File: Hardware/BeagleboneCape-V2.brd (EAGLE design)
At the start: 73.6 x 58.1 mm, 11 parts, among them P8 HEADER1, P9 HEADER2

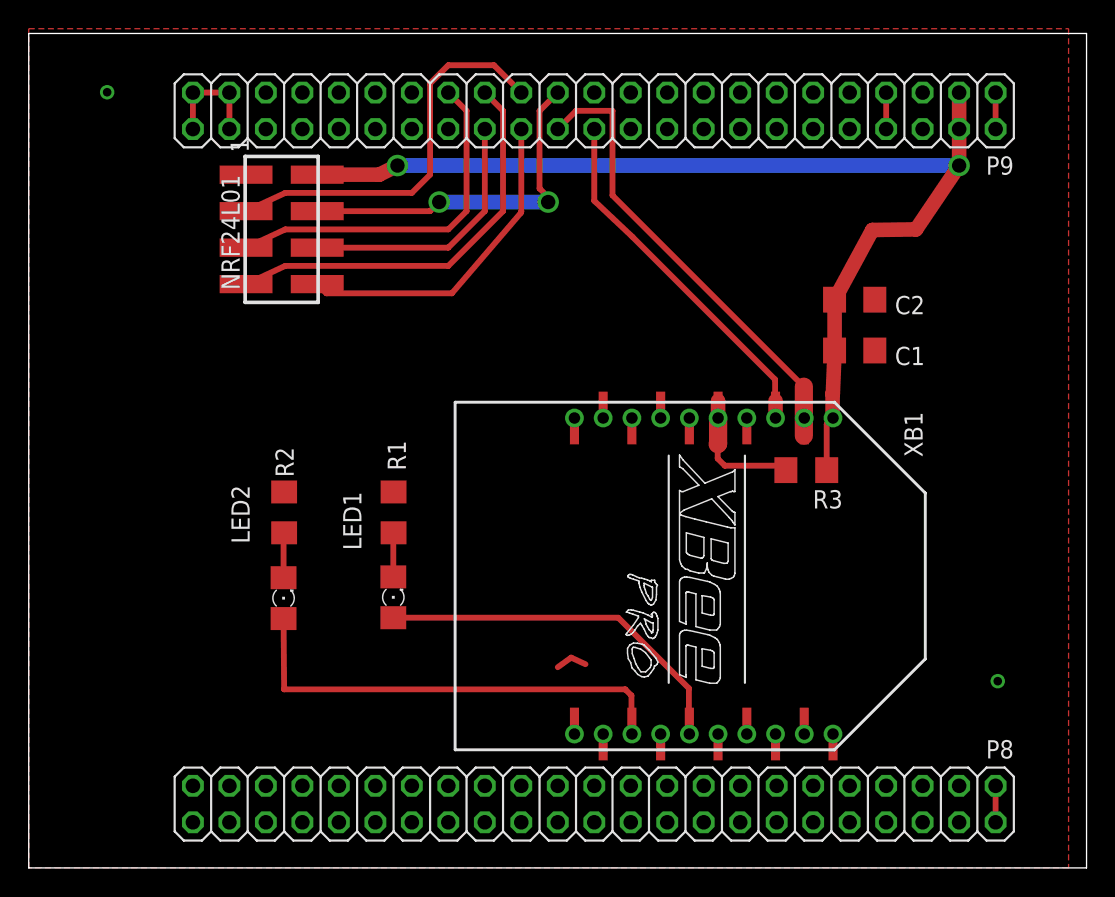
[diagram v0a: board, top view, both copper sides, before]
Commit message: updated beaglebone cape and added pdf build files
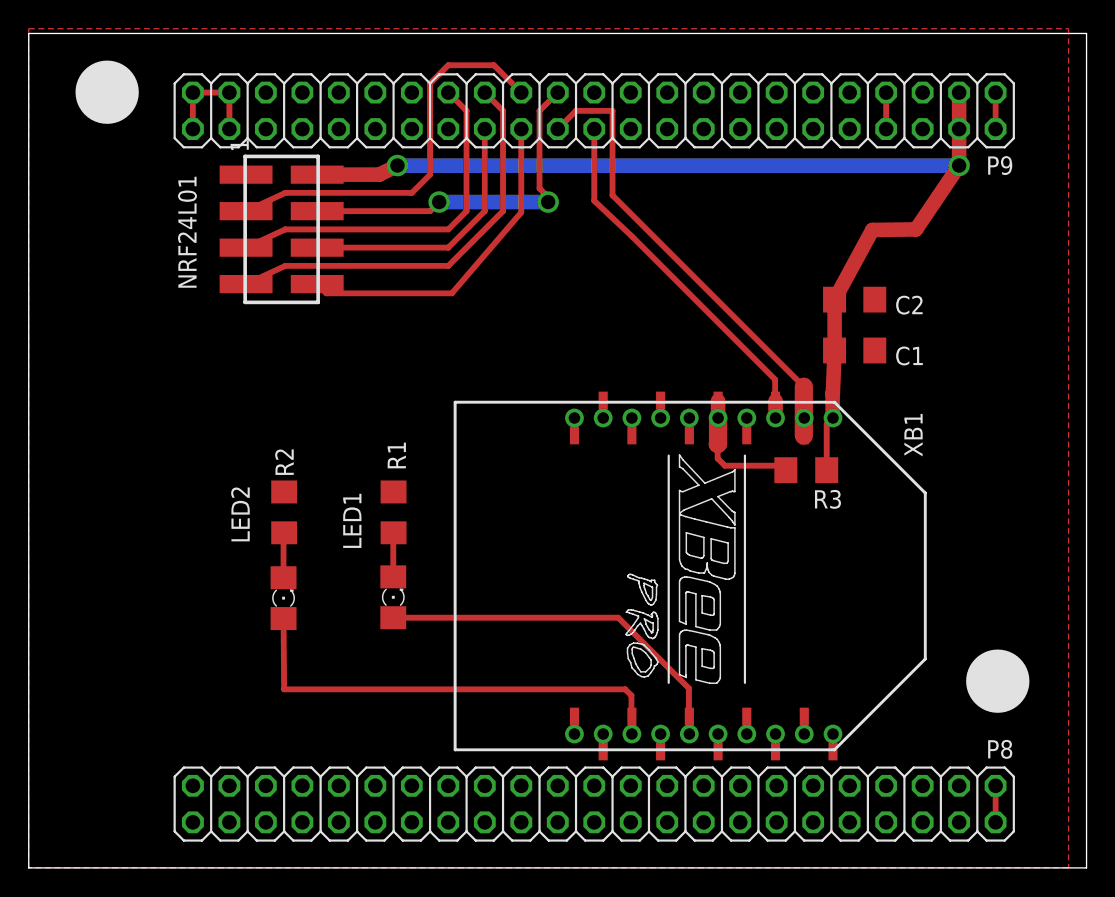
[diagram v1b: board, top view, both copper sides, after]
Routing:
- net GND: track 15.0 -> 12.7 mm
